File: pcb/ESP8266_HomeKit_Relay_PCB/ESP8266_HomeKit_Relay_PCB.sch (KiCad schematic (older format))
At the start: 19 parts, among them J1 ESP8266EX(ESP-01)

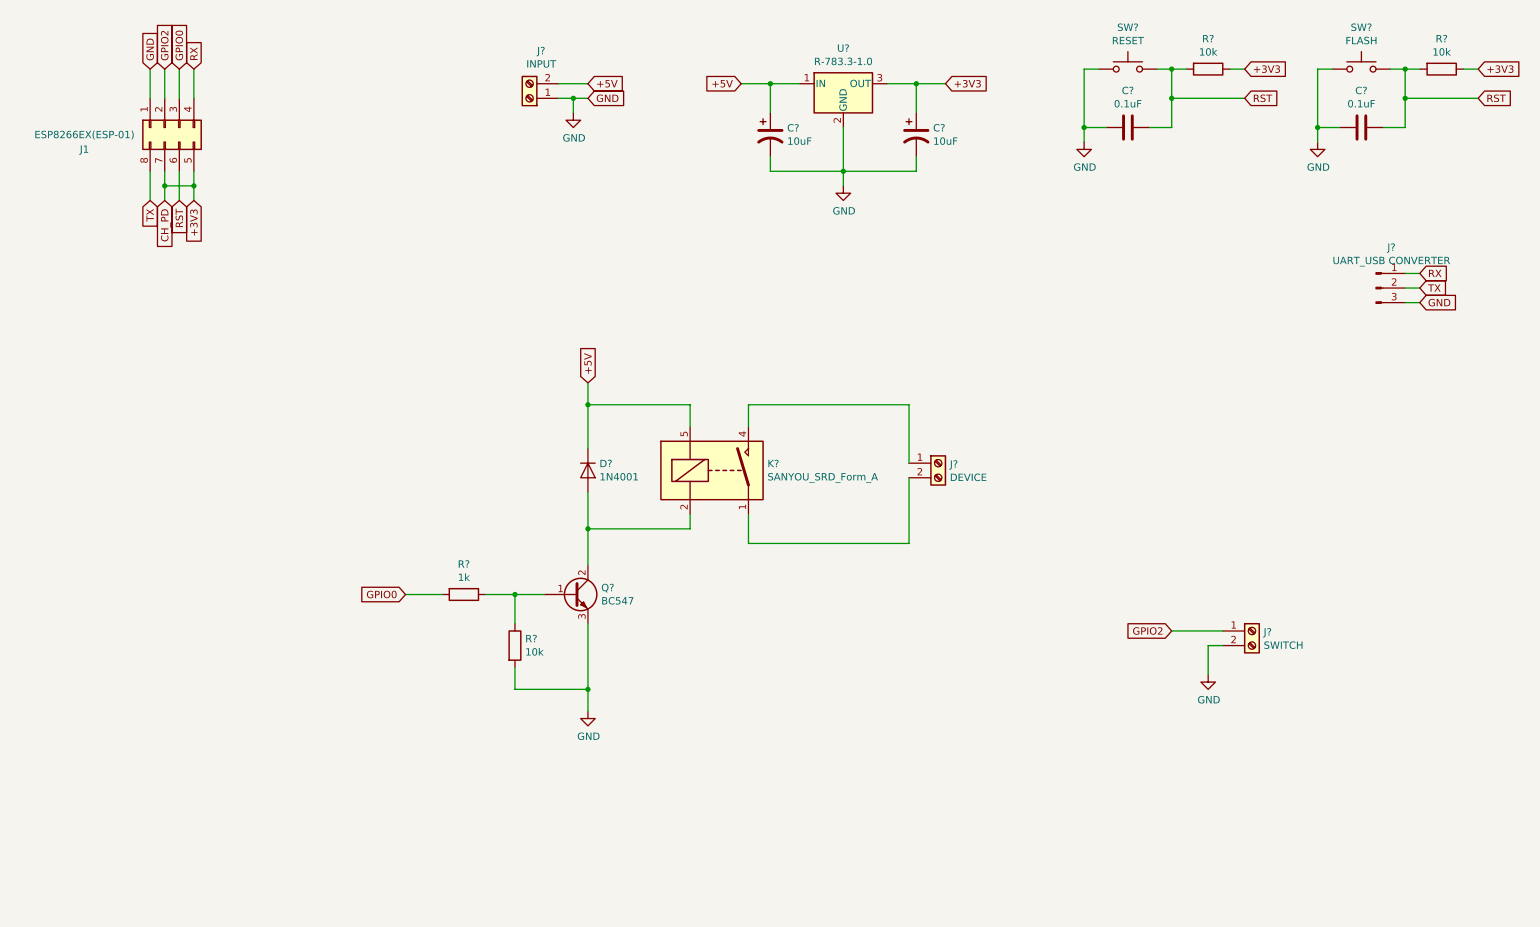
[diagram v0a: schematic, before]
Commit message: Button is detected. LED work with homekit
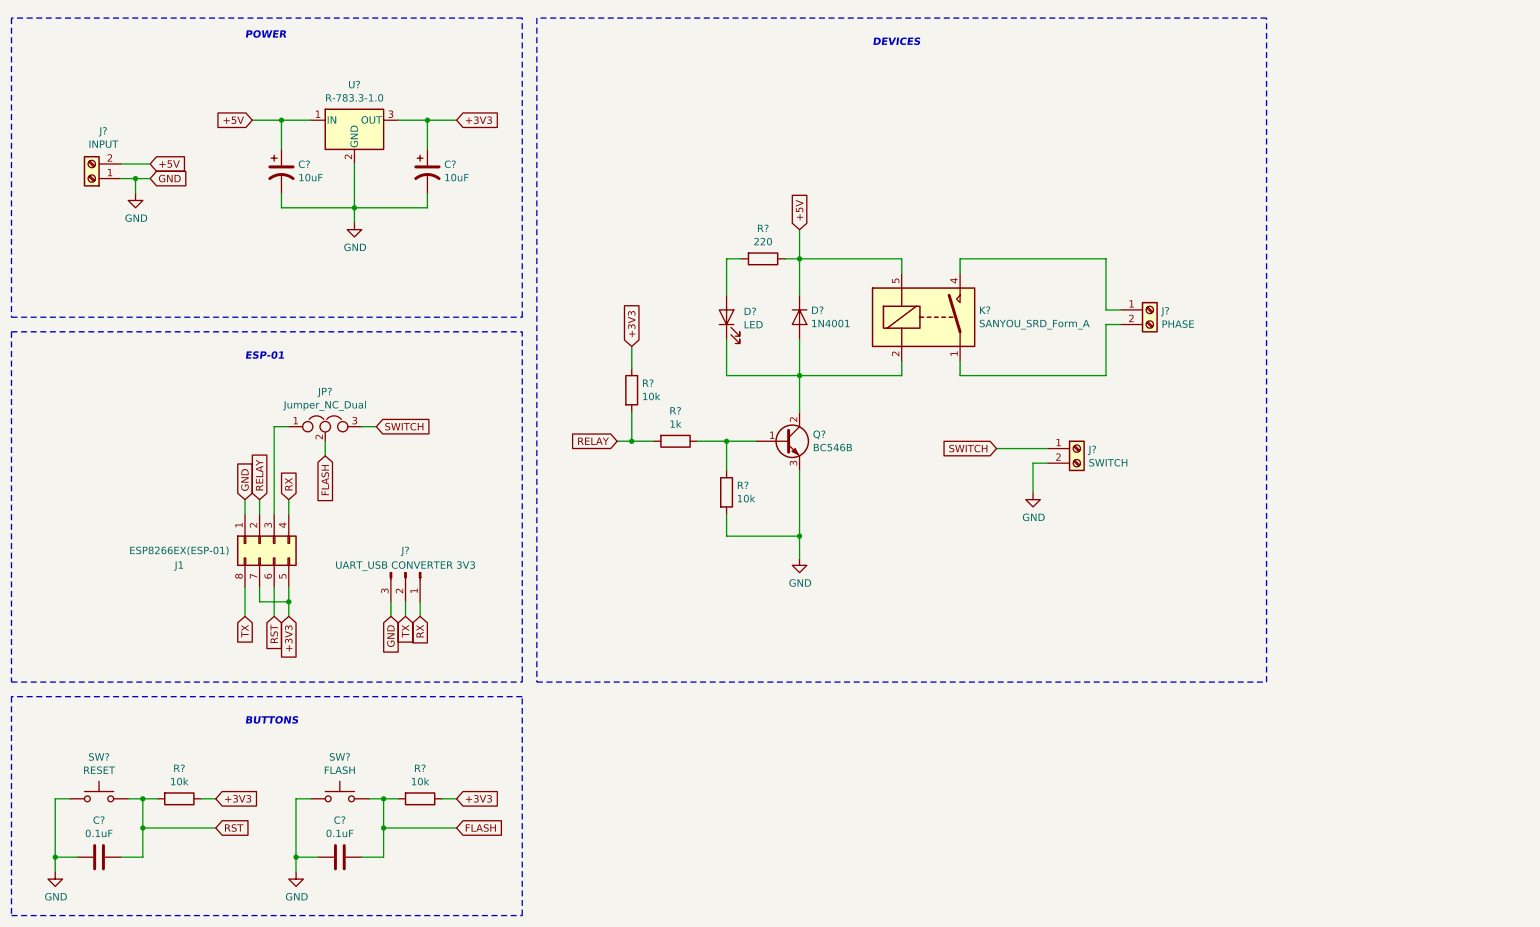
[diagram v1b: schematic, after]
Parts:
- added D?: LED, symbol Device:LED
- added JP?: Jumper_NC_Dual, symbol Device:Jumper_NC_Dual
- added R?: 220, symbol Device:R
- added R?: 10k, symbol Device:R
- J?: value UART_USB CONVERTER -> UART_USB CONVERTER 3V3
- J?: value DEVICE -> PHASE
- Q?: value BC547 -> BC546B
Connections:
- net +3V3: now also R?.1
- net +5V: now also R?.1
- net RST: no longer C?.1, R?.2, SW?.2
- net at D?.2 (A), K?.2, Q?.2 (C): now also D?.1 (K)
- net GPIO0: no longer names the net of J1.3 (Pin_3)
- net GPIO0: now also JP?.1; no longer R?.2
- net GPIO2 renamed RELAY
- net RELAY: now also R?.2, R?.2; no longer J?.1 (Pin_1)
- new net: D?.2 (A), R?.2
- new net FLASH: C?.1, JP?.2, R?.2, SW?.2
- new net SWITCH: J?.1 (Pin_1), JP?.3
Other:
- note added: "BUTTONS"
- note added: "DEVICES"
- note added: "ESP-01"
- note added: "POWER"
- moved on the sheet: C?, D?, J1, J?, K?, Q?, R?, SW?, U?
